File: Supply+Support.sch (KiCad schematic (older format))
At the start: 27 parts, among them J5 WP, J6 +5V Source, U2 M24128, U3 TLV755P

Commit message: Added the OSHW logo to the silkscreen for the board
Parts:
- added LOGO1: Logo_Open_Hardware_Small, Symbol:OSHW-Logo2_7.3x6mm_SilkScreen, symbol Graphic:Logo_Open_Hardware_Small
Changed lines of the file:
@@
 Wire Wire Line
 	5350 3550 5350 3450
+$Comp
+L Graphic:Logo_Open_Hardware_Small LOGO1
+U 1 1 5F02A9BA
+P 10500 1000
+F 0 "LOGO1" H 10500 1275 50  0001 C CNN
+F 1 "Logo_Open_Hardware_Small" H 10500 775 50  0001 C CNN
+F 2 "Symbol:OSHW-Logo2_7.3x6mm_SilkScreen" H 10500 1000 50  0001 C CNN
+F 3 "~" H 10500 1000 50  0001 C CNN
+	1    10500 1000
+	1    0    0    -1
+$EndComp
 $EndSCHEMATC

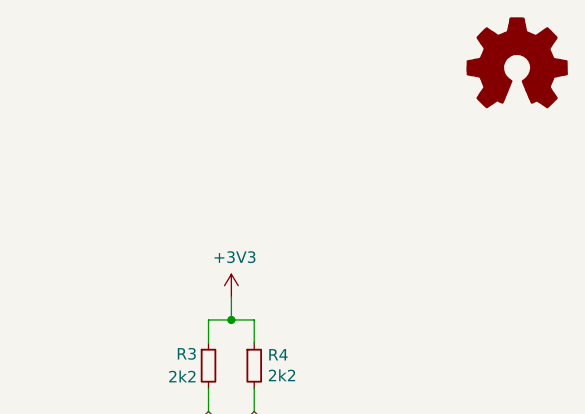
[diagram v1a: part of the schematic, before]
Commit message: Added some PCB art in the form of Tohru and Nagadreth
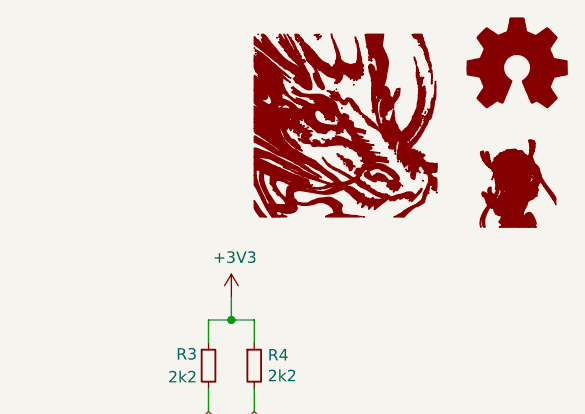
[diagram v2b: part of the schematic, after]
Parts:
- added DRG1: トール, トール:トール-12.9x14.8, symbol DX_MON:トール
- added DRG2: Nagadreth, Nagadreth:Nagadreth-12.0x12.0, symbol DX_MON:Nagadreth
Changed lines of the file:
@@
+	1    0    0    -1
+$EndComp
+$Comp
+L DX_MON:トール DRG1
+U 1 1 5F09BBD5
+P 10500 1500
+F 0 "DRG1" H 10500 1336 60  0001 C CNN
+F 1 "トール" H 10500 1664 60  0001 C CNN
+F 2 "トール:トール-12.9x14.8" H 10500 1500 59  0001 C CNN
+F 3 "" H 10500 1500 59  0001 C CNN
+	1    10500 1500
+	1    0    0    -1
+$EndComp
+$Comp
+L DX_MON:Nagadreth DRG2
+U 1 1 5F092D2D
+P 9750 1250
+F 0 "DRG2" H 9750 800 60  0001 C CNN
+F 1 "Nagadreth" H 9750 1700 60  0001 C CNN
+F 2 "Nagadreth:Nagadreth-12.0x12.0" H 9750 1250 59  0001 C CNN
+F 3 "" H 9750 1250 59  0001 C CNN
+	1    9750 1250
 	1    0    0    -1
 $EndComp
